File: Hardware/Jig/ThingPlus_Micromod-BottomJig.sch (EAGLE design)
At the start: 39 parts, among them J4 USB_A_PTH_MALE, J5 USB_A_SMT_FEMALE, U2 74LVC4066, U3 74LVC4066, U5 74LVC4066_MUX_1:1_X4

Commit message: Preliminary version of test jig bottom board uploaded
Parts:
- removed F1: 6V/2A, SparkFun-Fuses:PPTC_6V2A
- removed J4: USB_A_PTH_MALE, SparkFun-Connectors:USB_A_PTH_MALE
- removed J_SCL3, J_SCL4, J_SCL5, J_SDA1: JUMPER-SMT_2_NO_SILK, SparkFun-Jumpers:JUMPER-SMT_2_NO_SILK
- removed U$81: TB_MAIN_BRAIN_CARDEDGE_TB_SIDE, Testing:TB_MAIN_BRAIN_CARDEDGE_TB_SIDE
- removed U3: 74LVC4066, SparkFun-IC-Logic:74LVC4066D_QUAD_BILATERAL_SWITCH
- removed U5: 74LVC4066_MUX_1:1_X4, Testing:74LVC4066_MUX_1:1_X4
- added C1, C2: 0.1uF, SparkFun-Capacitors:0.1UF-0603-25V-(+80/-20%)
- added J1: USB_A_PTH_MALE, SparkFun-Connectors:USB_A_PTH_MALE
- added J7: QWIIC_RIGHT_ANGLE, SparkFun-Connectors:QWIIC_CONNECTORJS-1MM
- added LOGO2: OSHW-LOGOMINI, SparkFun-Aesthetics:OSHW-LOGOMINI
- added LOGO4: QWIIC_LOGO_4MM, SparkFun-Aesthetics:QWIIC_LOGO_4MM
- added U$1: SPARKX-LOGO4, SparkX:SPARKX-LOGO4
- added U1: TB_MAIN_BRAIN_CARDEDGE_TB_SIDE, Testing:TB_MAIN_BRAIN_CARDEDGE_TB_SIDE
- added U4: 74LVC4066_MUX_1:1_X4, Testing:74LVC4066_MUX_1:1_X4
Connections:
- removed net !BOOT!: J2.1
- removed net !RST!: J2.16
- removed net 3.3V: J2.15
- removed net A0: J2.12
- removed net A1: J2.11
- removed net D0: J2.8
- removed net D1: J2.7
- removed net EN: J3.11
- removed net G0: J3.9
- removed net G1: J3.8
- removed net G2: J3.7
- removed net G3: J3.6
- removed net G4: J3.5
- removed net G5: J3.4
- removed net G6: J3.3
- removed net J_10: U$81.10
- removed net J_11: U$81.11
- removed net J_12: U$81.12
- removed net J_13: U$81.13
- removed net J_14: U$81.14(TX3)
- removed net J_15: U$81.15(RX3)
- removed net J_16: U$81.16(TX2)
- removed net J_17: U$81.17(RX2)
- removed net J_2: U$81.2(INT0)
- removed net J_27: U$81.27
- removed net J_28: U$81.28
- removed net J_29: U$81.29
- removed net J_3: U$81.3(INT1)
- removed net J_5: U$81.5
- removed net J_6: U$81.6
- removed net J_7: U$81.7
- removed net J_8: U$81.8
- removed net J_9: U$81.9
- removed net J_A1: U$81.A1
- removed net J_A10: U$81.A10
- removed net J_A11: U$81.A11
- removed net J_A12: U$81.A12
- removed net J_A2: U$81.A2
- removed net J_A3: U$81.A3
- removed net J_A4: U$81.A4
- removed net J_A5: U$81.A5
- removed net J_A6: U$81.A6
- removed net J_A7: U$81.A7
- removed net J_A8: U$81.A8
- removed net J_A9: U$81.A9
- removed net PWM0: J2.10
- removed net PWM1: J2.9
- removed net SCL/G7: J3.2
- removed net SDA: J3.1
- removed net SPI_CIPO: J2.4
- removed net SPI_COPI: J2.5
- removed net SPI_SCK: J2.6
- removed net TARGET_CIPO: J_SCL5.2, U3.1Z
- removed net TARGET_COPI: J_SCL3.2, U3.2Z
- removed net TARGET_CS: J_SDA1.2, U3.4Z
- removed net TARGET_RX: J_SCL1.2, U2.3Z
- removed net TARGET_SCK: J_SCL4.2, U3.3Z
- removed net TARGET_SCL: J_SCL.2, U2.2Z
- removed net TARGET_SDA: J_SCL2.2, U2.1Z
- removed net TARGET_TX: J_SDA.2, U2.4Z
- removed net UART_RX: J2.3
- removed net UART_TX: J2.2
- removed net V_BATT: J3.12
- removed net V_USB: J3.10
- new net !MICROMOD_BOOT!: J2.1, U1.17(RX2)
- new net !MICROMOD_RST!: J2.16, U1.A3
- new net BRD_USB_D+: J5.D-, U4.1Z
- new net BRD_USB_D-: J5.D+, U4.2Z
- new net J_19: U1.16(TX2)
- new net J_30: U1.12
- new net J_34: U1.11
- new net J_38: U1.10
- new net J_42: U1.29
- new net J_46: U1.28
- new net J_50: U1.27
- new net J_58: U1.25
- new net MICROMOD_3V3: J2.15, U1.A1
- new net MICROMOD_A0: J2.12, U1.A5
- new net MICROMOD_A1: J2.11, U1.A6
- new net MICROMOD_CIPO: J2.4, U1.15(RX3)
- new net MICROMOD_COPI: J2.5, U1.8
- new net MICROMOD_D0: J2.8, U1.A11
- new net MICROMOD_D1: J2.7, U1.2(INT0)
- new net MICROMOD_EN: J3.11, U1.A4
- new net MICROMOD_G0: J3.9, U1.A8
- new net MICROMOD_G1: J3.8, U1.A10
- new net MICROMOD_G2: J3.7, U1.A12
- new net MICROMOD_G3: J3.6, U1.3(INT1)
- new net MICROMOD_G4: J3.5, U1.5
- new net MICROMOD_G5: J3.4, U1.6
- new net MICROMOD_G6: J3.3, U1.14(TX3)
- new net MICROMOD_PWM0: J2.10, U1.A7
- new net MICROMOD_PWM1: J2.9, U1.A9
- new net MICROMOD_QWIIC_PWR: J7.2, U1.A2
- new net MICROMOD_RX: J2.2, J_SCL1.2, U2.3Z
- new net MICROMOD_SCK: J2.6, U1.7
- new net MICROMOD_SCL: J3.2, J_SCL.2, U2.2Z
- new net MICROMOD_SDA: J3.1, J_SCL2.2, U2.1Z
- new net MICROMOD_TX: J2.3, J_SDA.2, U2.4Z
- new net NC: J5.VBUS
- new net USB_D+: J1.D+, U4.1Y
- new net USB_D-: J1.D-, U4.2Y
- new net USB_SWCH_EN: U1.26, U4.1E, U4.2E
- net BRAIN_VCC: now also C1.1, C2.1, U1.BRAIN_VCC, U4.VCC; no longer U$81.BRAIN_VCC, U3.VCC
- net BRAIN_VCC_A0: now also U1.A0; no longer U$81.A0
- net FAILURE_LED: now also U1.43/LED4; no longer U$81.43/LED4
- net GND: now also C1.2, C2.2, J1.GND, J5.GND, J7.1, U1.GND, U4.3E, U4.4E, U4.GND; no longer U$81.GND, U3.GND
- net J_25: now also U1.9; no longer U$81.25
- net J_26: now also U1.13; no longer U$81.26
- net J_CIPO: now also U1.50; no longer J_SCL5.1, U$81.50, U3.1Y
- net J_COPI: now also U1.51; no longer J_SCL3.1, U$81.51, U3.2Y
- net J_CS: now also U1.53; no longer J_SDA1.1, U$81.53, U3.4Y
- net J_I2C_EN: now also U1.22; no longer U$81.22
- net J_MICROSD_!CS!: now also U1.49; no longer U$81.49
- net J_MICROSD_EN: now also U1.47; no longer U$81.47
- net J_MICROSD_PWR_EN: now also U1.30; no longer U$81.30
- net J_RX1-I: now also U1.19(RX1/INT4); no longer U$81.19(RX1/INT4)
- net J_SCK: now also U1.52; no longer J_SCL4.1, U$81.52, U3.3Y
- net J_SCL: now also U1.21(SCL/INT2); no longer U$81.21(SCL/INT2)
- net J_SDA: now also U1.20(SDA/INT3); no longer U$81.20(SDA/INT3)
- net J_SERIAL_EN: now also U1.23; no longer U$81.23
- net J_SPI_EN: now also U1.24; no longer U$81.24, U3.1E, U3.2E, U3.3E, U3.4E
- net J_TX1-O: now also U1.18(TX1/INT5); no longer U$81.18(TX1/INT5)
- net MT_PASS_LED: now also U1.42/LED3; no longer U$81.42/LED3
- net N$1: now also U1.31/CS_RETURN; no longer U$81.31/CS_RETURN
- net N$15: now also U1.45/CS1; no longer U$81.45/CS1
- net N$18: now also U1.46/CS2; no longer U$81.46/CS2
- net PT_PASS_LED: now also U1.40/LED1; no longer U$81.40/LED1
- net RAW: now also U1.RAW; no longer U$81.RAW
- net STAT_LED: now also U1.41/LED2; no longer U$81.41/LED2
- net V1: now also J3.10, U1.V1; no longer U$81.V1
- net V2: now also J3.12, U1.V2; no longer U$81.V2
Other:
- moved on the sheet: BUTTON1, BUTTON2, D1, FAIL, J2, J3, J5, JP1, JP2, MT_PASS, PT_PASS, R1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

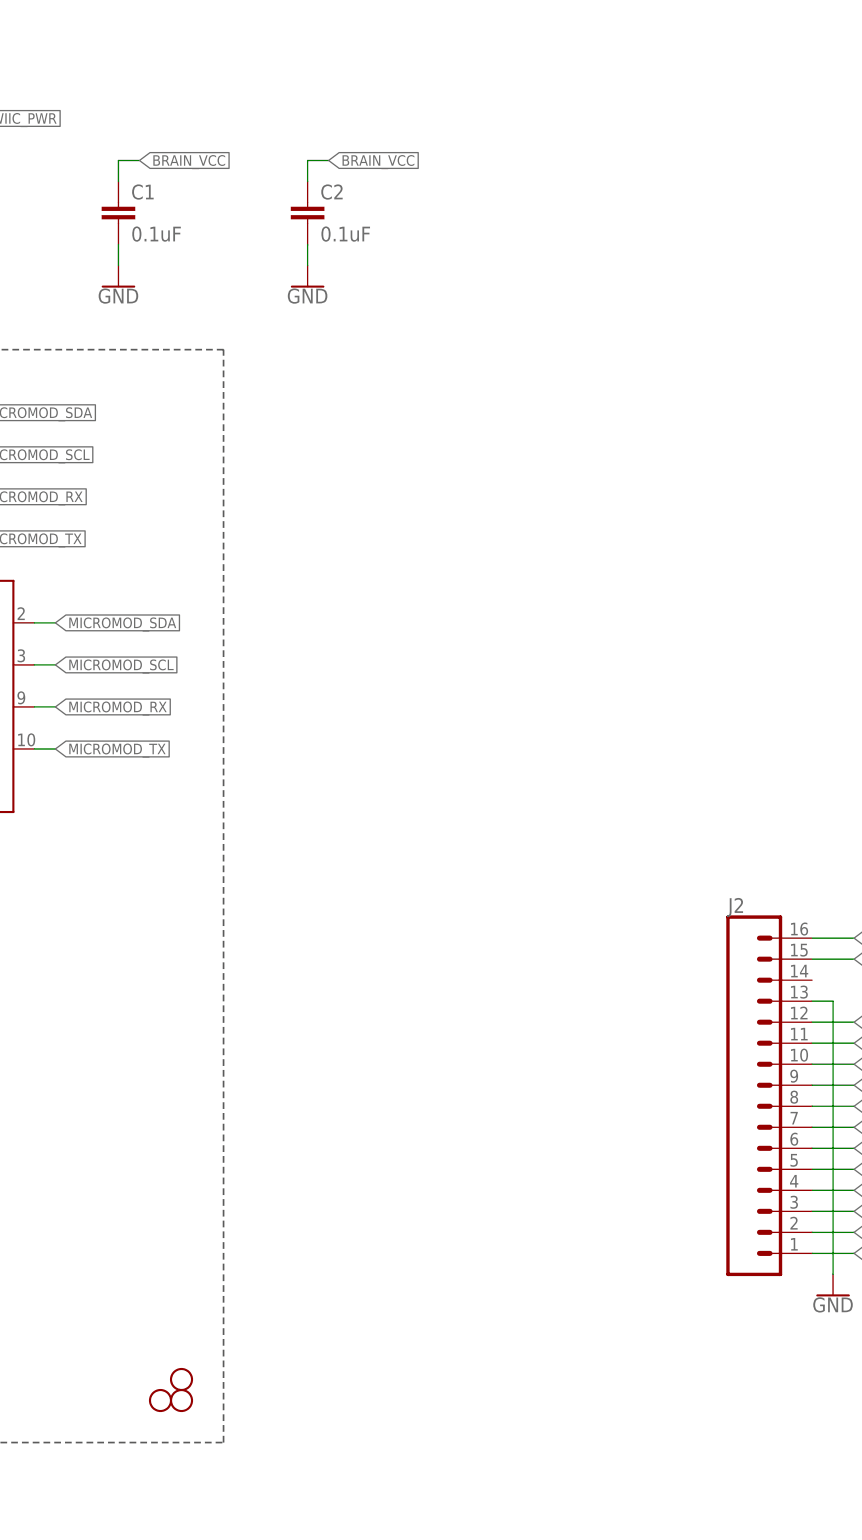
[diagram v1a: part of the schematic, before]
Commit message: Moved touch pad traces; added missing mounting hole; created top and middle jig boards;
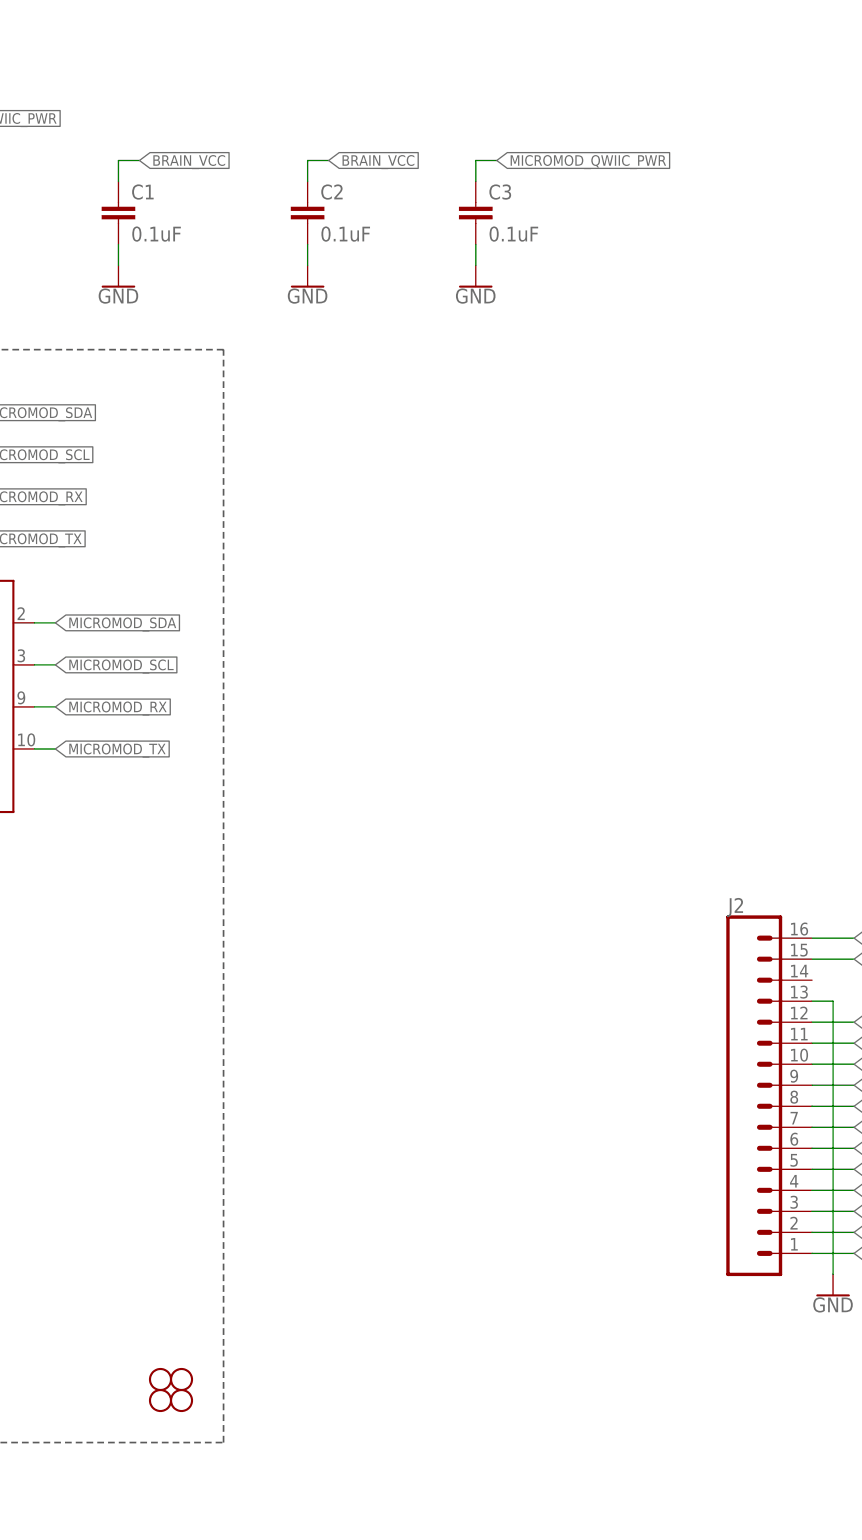
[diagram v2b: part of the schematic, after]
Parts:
- added C3: 0.1uF, SparkFun-Capacitors:0.1UF-0603-25V-(+80/-20%)
- added H5: STAND-OFF, SparkFun-Hardware:STAND-OFF
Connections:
- net GND: now also C3.2
- net MICROMOD_QWIIC_PWR: now also C3.1
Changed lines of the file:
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@@
 <setting verticaltext="up"/>
 </settings>
-<grid distance="0.1" unitdist="inch" unit="inch" style="lines" multiple="1" display="yes" altdistance="0.005" altunitdist="inch" altunit="inch"/>
+<grid distance="0.1" unitdist="inch" unit="inch" style="lines" multiple="1" display="no" altdistance="0.01" altunitdist="inch" altunit="inch"/>
 <layers>
 <layer number="1" name="Top" color="4" fill="1" visible="no" active="no"/>
@@
 <part name="GND6" library="SparkFun-PowerSymbols" deviceset="GND" device=""/>
 <part name="GND7" library="SparkFun-PowerSymbols" deviceset="GND" device=""/>
+<part name="C3" library="SparkFun-Capacitors" deviceset="0.1UF" device="-0603-25V-(+80/-20%)" value="0.1uF"/>
+<part name="GND8" library="SparkFun-PowerSymbols" deviceset="GND" device=""/>
+<part name="H5" library="SparkFun-Hardware" deviceset="STAND-OFF" device=""/>
 </parts>
 <sheets>
@@
 <attribute name="VALUE" x="264.16" y="187.706" size="1.778" layer="96" align="top-center"/>
 </instance>
+<instance part="C3" gate="G$1" x="284.48" y="195.58" smashed="yes">
+<attribute name="NAME" x="286.004" y="198.501" size="1.778" layer="95" font="vector"/>
+<attribute name="VALUE" x="286.004" y="193.421" size="1.778" layer="96" font="vector"/>
+</instance>
+<instance part="GND8" gate="1" x="284.48" y="187.96" smashed="yes">
+<attribute name="VALUE" x="284.48" y="187.706" size="1.778" layer="96" align="top-center"/>
+</instance>
+<instance part="H5" gate="G$1" x="246.38" y="55.88" smashed="yes"/>
 </instances>
 <busses>
@@
 <pinref part="GND7" gate="1" pin="GND"/>
 </segment>
+<segment>
+<pinref part="C3" gate="G$1" pin="2"/>
+<wire x1="284.48" y1="193.04" x2="284.48" y2="190.5" width="0.1524" layer="91"/>
+<pinref part="GND8" gate="1" pin="GND"/>
+</segment>
 </net>
 <net name="MICROMOD_PWM0" class="0">
@@
 <label x="213.36" y="208.28" size="1.27" layer="95" xref="yes"/>
 </segment>
-</net>
+<segment>
+<pinref part="C3" gate="G$1" pin="1"/>
+<wire x1="284.48" y1="200.66" x2="284.48" y2="203.2" width="0.1524" layer="91"/>
+<wire x1="284.48" y1="203.2" x2="287.02" y2="203.2" width="0.1524" layer="91"/>
+<label x="287.02" y="203.2" size="1.27" layer="95" xref="yes"/>
+</segment>
+</net>
